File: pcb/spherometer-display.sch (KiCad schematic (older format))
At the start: 14 parts, among them J1 Battery, J2 Indicator, J3 Disp, J4 Programming, Q1 NPN, Q2 NPN, SW1 UI-Button, U1 ATTINY85V-10SU

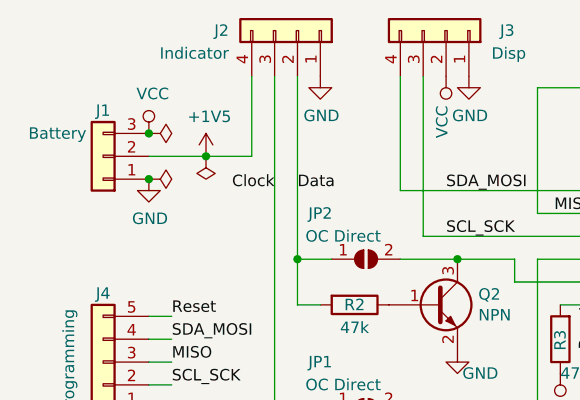
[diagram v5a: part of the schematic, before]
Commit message: New tactile button; slot-access cables; cutouts for components below.
o The old tactile button was too small and flimsy and disintegrated
  quickly. Use a new one.
o Cables are not connected anymore with JST connectors (too big), but
  instead slots are provided to solder them in. Also, some space
  above the board is provided for the cable access to minimize space-loss
  due to discomboulated cable entrance.
o Provide cutouts for places where on the 1.3" displays typically components
  are to be found.
o Make the board slightly less high as the row of passives in some displays
  starts a bit further up.

This is work-in-progress. Cleanup of silk-screen has to be done and
cut-outs need to be prettified. Also, GND is not connected everywhere yet.
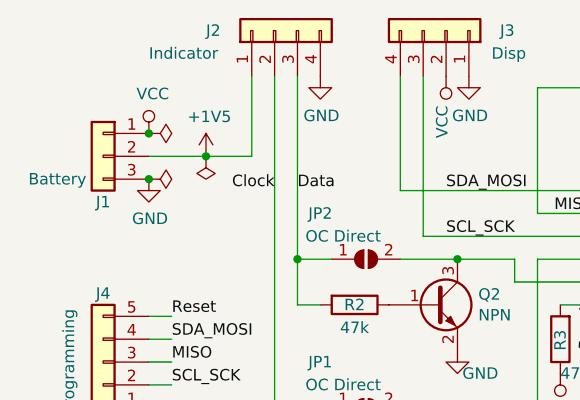
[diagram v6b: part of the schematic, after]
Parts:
- J1: footprint Connector_JST:JST_PH_S3B-PH-K_1x03_P2.00mm_Horizontal -> digi-spherometer:connect-edge-3slot-2mm
- J2: footprint Connector_JST:JST_PH_S4B-PH-K_1x04_P2.00mm_Horizontal -> digi-spherometer:connect-edge-4slot-2mm
- SW1: footprint digi-spherometer:EVPAV-Switch -> digi-spherometer:EVQP7-Switch
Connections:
- net +1V5: now also J2.1 (Pin_1); no longer J2.4 (Pin_4)
- net Clock: now also J2.2 (Pin_2); no longer J2.3 (Pin_3)
- net Data: now also J2.3 (Pin_3); no longer J2.2 (Pin_2)
- net GND: now also J1.3 (Pin_3), J2.4 (Pin_4); no longer J1.1 (Pin_1), J2.1 (Pin_1)
- net VCC: now also J1.1 (Pin_1); no longer J1.3 (Pin_3)
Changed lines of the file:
@@
 F 0 "SW1" H 3450 2600 50  0000 C CNN
 F 1 "UI-Button" H 3300 2500 50  0000 C CNN
-F 2 "digi-spherometer:EVPAV-Switch" H 3650 2650 50  0001 C CNN
+F 2 "digi-spherometer:EVQP7-Switch" H 3650 2650 50  0001 C CNN
 F 3 "" H 3650 2650 50  0001 C CNN
 	1    3650 2450
@@
 L Connector_Generic:Conn_01x04 J2
 U 1 1 5C7C8F49
-P 2150 2200
-F 0 "J2" V 2150 1900 50  0000 R CNN
-F 1 "Indicator" V 2050 1900 50  0000 R CNN
-F 2 "Connector_JST:JST_PH_S4B-PH-K_1x04_P2.00mm_Horizontal" H 2150 2200 50  0001 C CNN
-F 3 "~" H 2150 2200 50  0001 C CNN
-	1    2150 2200
-	0    1    -1   0
+P 2050 2200
+F 0 "J2" V 2050 2500 50  0000 R CNN
+F 1 "Indicator" V 1950 2750 50  0000 R CNN
+F 2 "digi-spherometer:connect-edge-4slot-2mm" H 2050 2200 50  0001 C CNN
+F 3 "~" H 2050 2200 50  0001 C CNN
+	1    2050 2200
+	0    -1   -1   0
 $EndComp
 $Comp
@@
 F 0 "J1" H 1300 2550 50  0000 C CNN
 F 1 "Battery" H 1500 2650 50  0000 C CNN
-F 2 "Connector_JST:JST_PH_S3B-PH-K_1x03_P2.00mm_Horizontal" H 1300 2750 50  0001 C CNN
+F 2 "digi-spherometer:connect-edge-3slot-2mm" H 1300 2750 50  0001 C CNN
 F 3 "~" H 1300 2750 50  0001 C CNN
 	1    1300 2750
-	-1   0    0    1
+	-1   0    0    -1
 $EndComp
 $Comp
